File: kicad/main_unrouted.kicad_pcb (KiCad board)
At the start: 2 copper layers, 162.2 x 137.3 mm, 46 parts, among them J1 Barrel_Jack, J2 UART, P1 Mini-DIN_6pins_ver3, SW1 Reset, U1 KM1810VM88, U10 L7805, U11 15 MHz, U12 8255, U13 uSD adapter, U15 74HC148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

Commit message: Add 8259 interrupt controller, update PCB
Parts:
- removed C13: 0.1 uF, footprints:C_Disc_Long
- removed U15: 74HC148, Package_DIP:DIP-16_W7.62mm_Socket
- removed U17: 74HC244, Package_DIP:DIP-20_W7.62mm_Socket
- added U14: 8259, Package_DIP:DIP-28_W15.24mm_Socket, F.Cu at (34.3, 76.2)
- C12: footprint footprints:C_Disc_Long -> footprints:C_Disc_VeryLong
- moved C12 180.2 mm to (41.9, 85.1)
- moved R5 147.3 mm to (23.6, 50.8)
- moved P1 146.6 mm to (30.2, 62.8)
- moved R4 144.8 mm to (23.6, 71.1)
- moved RN1 128.5 mm to (68.6, 119.4)
- moved U13 128.4 mm to (174.6, 113.0), turned to -90 degrees
- moved U18 127.8 mm to (131.9, 113.0)
- moved J2 127.6 mm to (120.7, 152.4)
- moved C9 127.6 mm to (108.6, 135.9)
- moved U16 127.6 mm to (92.7, 143.5)
- moved H1 127.1 mm to (25.4, 149.9)
- moved H2 127.1 mm to (177.8, 149.9)
- moved C11 127.1 mm to (26.7, 134.6)
- moved C14 127.1 mm to (153.7, 25.4)
- moved C6 127.1 mm to (132.0, 66.7)
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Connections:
- U12 pad 14: Net-(U12-PC0) -> INT1
- U16 pad 30: Net-(U16-INTR) -> INT4
- U6 pad 18: unconnected-(U6-I/O/Q-Pad18) -> INT~{EN}
- U8 pad 10: ~{INT1} -> unconnected-(U8-Pad10)
- U8 pad 11: Net-(U12-PC0) -> unconnected-(U8-Pad11)
- U8 pad 12: ~{INT2} -> unconnected-(U8-Pad12)
- U8 pad 13: Net-(U16-INTR) -> unconnected-(U8-Pad13)
- U8 pad 8: ~{INT0} -> unconnected-(U8-Pad8)
- U8 pad 9: Net-(U9-OUT0) -> unconnected-(U8-Pad9)
- U9 pad 10: Net-(U9-OUT0) -> INT0
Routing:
- net GND: track 277.4 -> 252.0 mm
- net +5V: track 191.2 -> 172.9 mm
- net ~{RES}: track 57.1 -> 46.1 mm
- net PS2CLK: track 8.82 -> 6.98 mm
- net PS2DATA: track 13.3 -> 12.6 mm
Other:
- board text added: "Андрій Дунай v0.2, Жовтень 2023 <a@dun.ai>"
- board text removed: "Андрій Дунай v0.2, Вересень 2023 <a@dun.ai>"

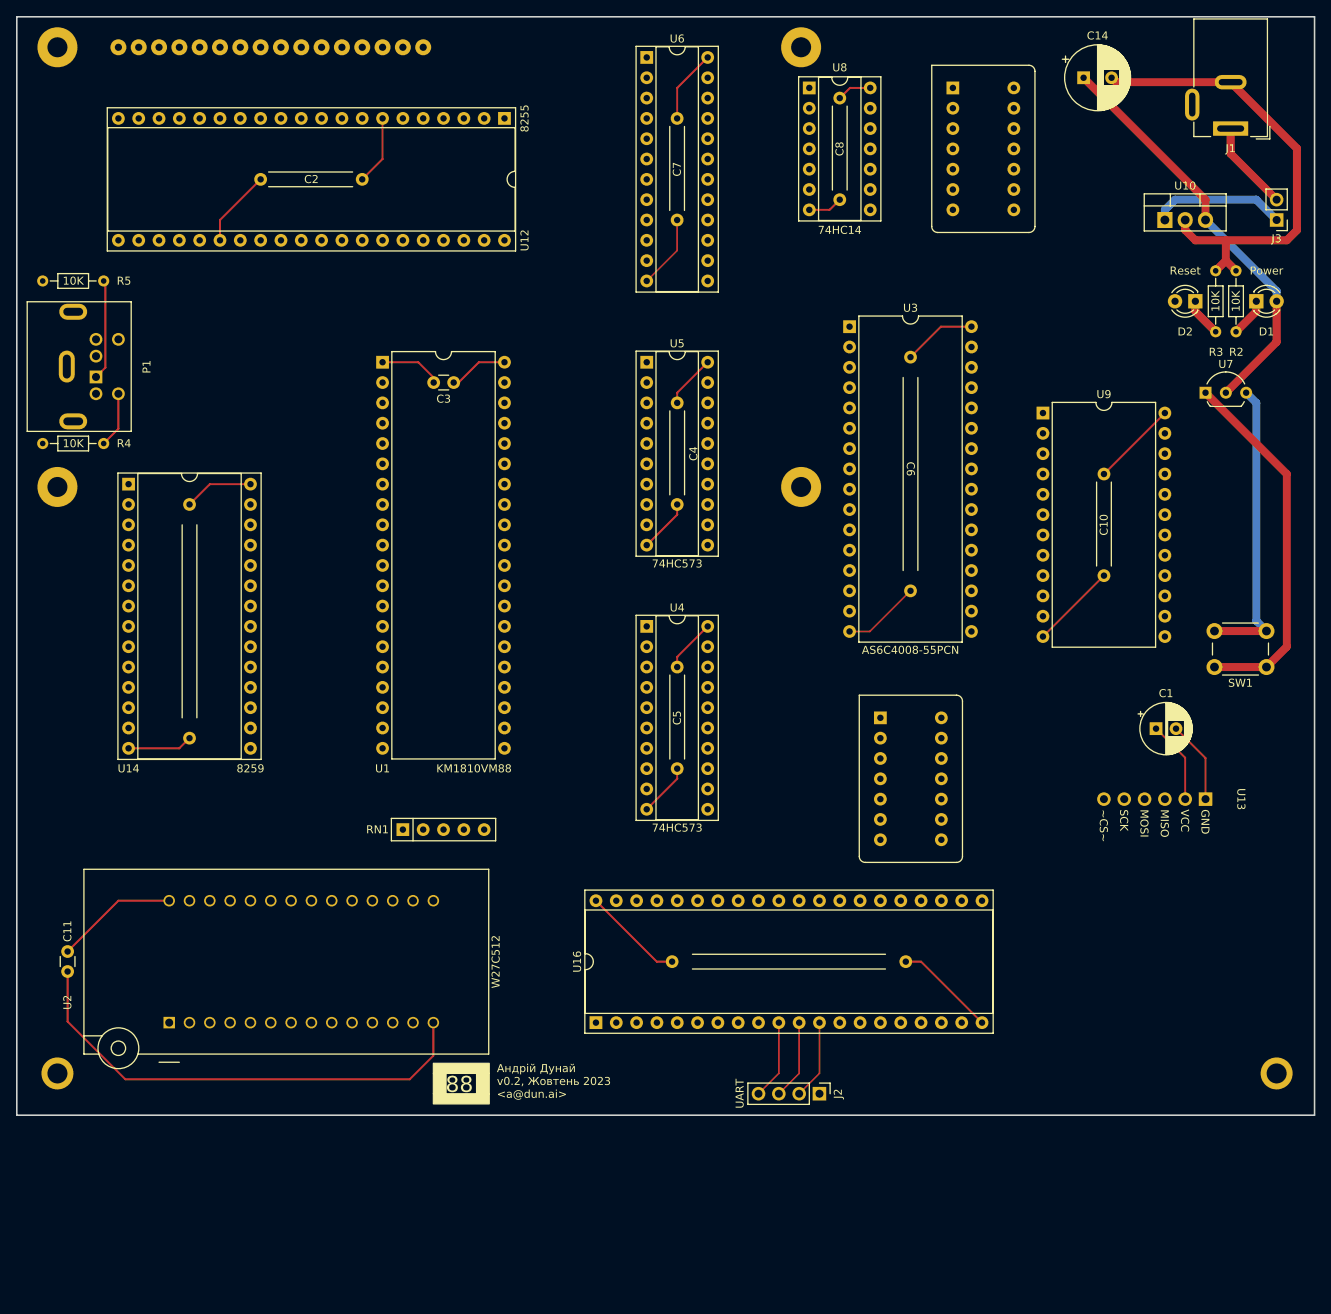
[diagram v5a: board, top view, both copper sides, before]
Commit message: 135x160 board
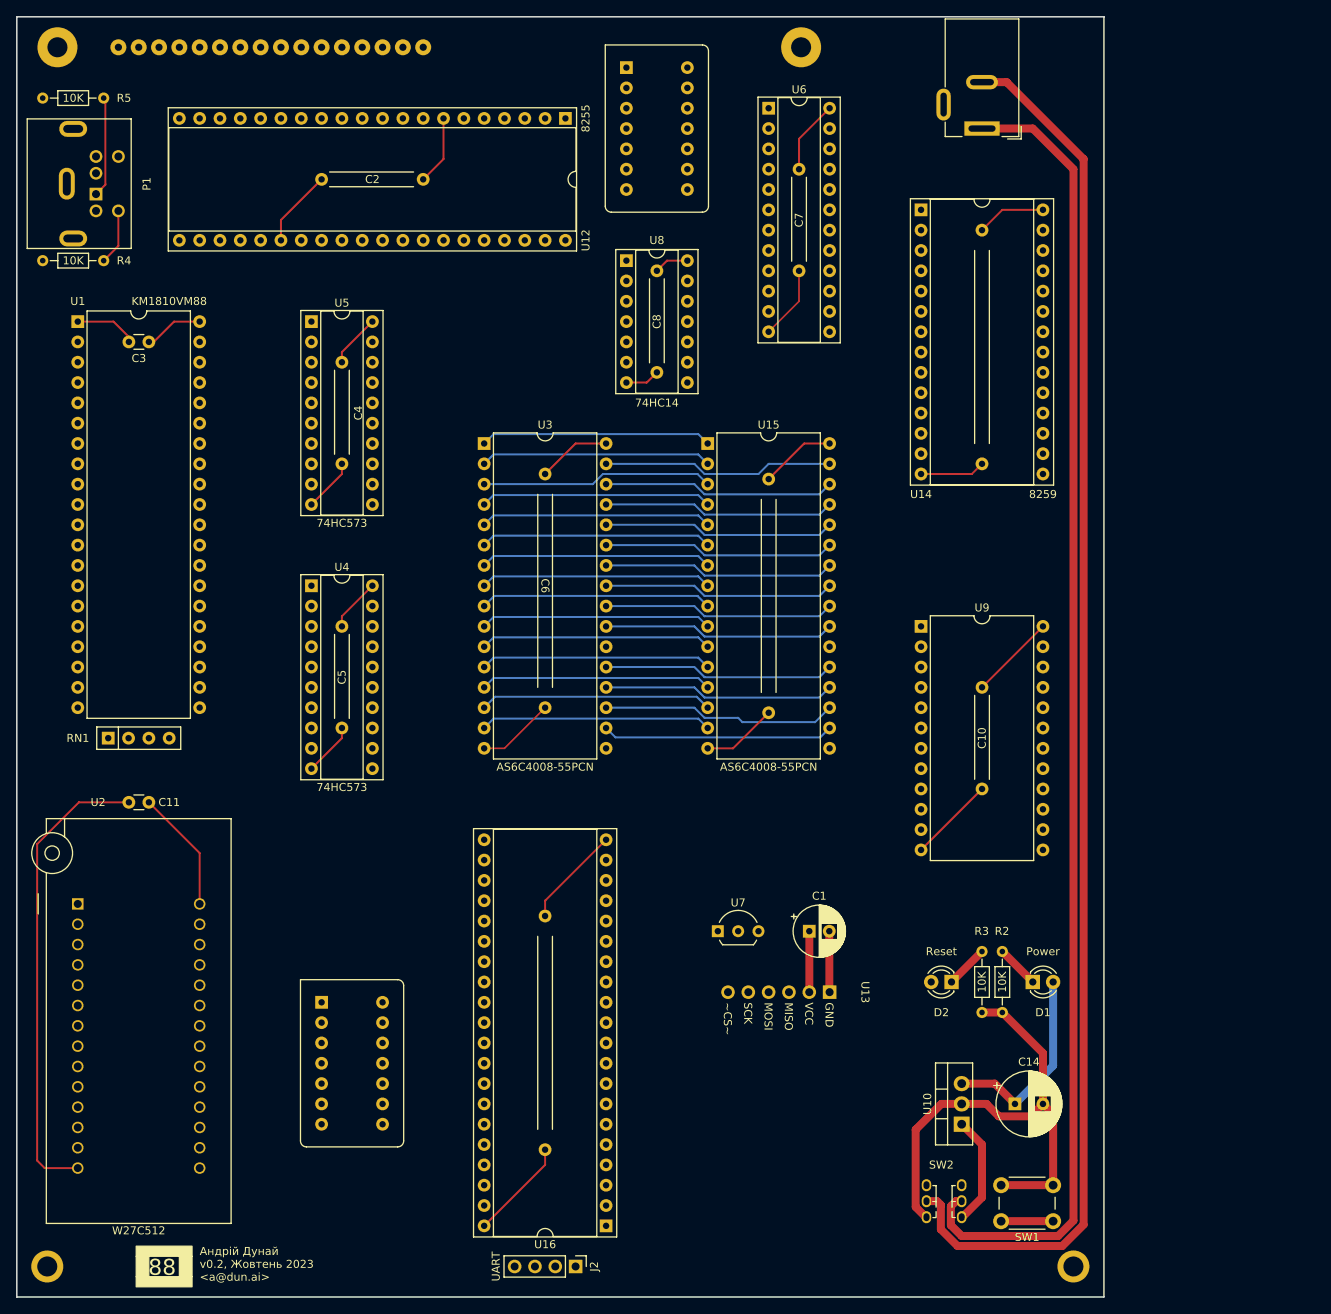
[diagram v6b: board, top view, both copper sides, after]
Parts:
- removed J3: ~, Connector_PinHeader_2.54mm:PinHeader_1x02_P2.54mm_Vertical
- added C13: 0.1 uF, footprints:C_Disc_VeryLong, F.Cu at (114.3, 81.9)
- added SW2: SW_Push_DPDT, footprints:PB22E06, F.Cu at (133.3, 163.0)
- added U15: AS6C4008-55PCN, Package_DIP:DIP-32_W15.24mm, F.Cu at (106.7, 71.1)
- RN1: value 5K -> R_Network03_Split; footprint Resistor_THT:R_Array_SIP5 -> Resistor_THT:R_Array_SIP4
- moved C14 128.6 mm to (145.1, 153.7)
- moved U10 115.8 mm to (138.4, 156.2), turned to 90 degrees
- moved C12 104.8 mm to (141.0, 50.8)
- moved U14 104.8 mm to (133.3, 41.9)
- moved U7 90.8 mm to (108.0, 132.1)
- moved D2 90.4 mm to (137.2, 138.4)
- moved D1 89.6 mm to (147.3, 138.4)
- moved R2 82.8 mm to (143.5, 134.6), turned to -90 degrees
- moved R3 82.8 mm to (141.0, 134.6), turned to -90 degrees
- moved U18 78.4 mm to (62.1, 148.6)
- moved SW1 74.2 mm to (149.9, 168.3)
- moved U13 52.8 mm to (127.6, 137.2)
- moved C1 50.2 mm to (119.4, 132.1)
- moved U3 48.0 mm to (78.7, 71.1)
- moved C6 48.0 mm to (86.4, 81.3)
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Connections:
- J1 pad 2: GND -> Net-(J1-Pad2)
- RN1 pad 4: unconnected-(RN1C-R3.2-Pad4) -> Net-(RN1C-R3.2)
- U1 pad 33: Net-(RN1D-R4.2) -> Net-(RN1C-R3.2)
- U12 pad 6: IO~{EN} -> PPI~{EN}
- U3 pad 22: RAM~{EN} -> LORAM~{EN}
- U6 pad 14: unconnected-(U6-I/O/Q-Pad14) -> HIRAM~{EN}
- U6 pad 15: Net-(U6-I/O/Q-Pad15) -> LORAM~{EN}
- U6 pad 16: Net-(U6-I/O/Q-Pad16) -> ROM~{EN}
- U6 pad 17: unconnected-(U6-I/O/Q-Pad17) -> INT~{EN}
- U6 pad 18: INT~{EN} -> UART~{EN}
- U6 pad 19: UART~{EN} -> TIMER~{EN}
- U6 pad 2: A_{8} -> A_{5}
- U6 pad 20: TIMER~{EN} -> PPI~{EN}
- U6 pad 21: IO~{EN} -> unconnected-(U6-I/O/Q-Pad21)
- U6 pad 22: RAM~{EN} -> Net-(U6-I/O/Q-Pad22)
- U6 pad 23: ROM~{EN} -> Net-(U6-I/O/Q-Pad23)
- U6 pad 3: A_{9} -> A_{6}
- U8 pad 1: Net-(U6-I/O/Q-Pad15) -> Net-(U6-I/O/Q-Pad23)
- U8 pad 2: CLK -> TIMERCLK
- U8 pad 3: Net-(U6-I/O/Q-Pad16) -> Net-(U6-I/O/Q-Pad22)
- U8 pad 4: TIMERCLK -> CLK
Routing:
- net Net-(J1-Pad2): track 0.00 -> 174.7 mm
- net Net-(J1-Pad1): track 11.3 -> 165.6 mm
- net ~{RES}: track 46.1 -> 6.50 mm
- net +5V: track 172.9 -> 142.6 mm
- net AD_{5}: track 0.00 -> 29.4 mm
- net AD_{1}: track 0.00 -> 29.1 mm
- net ~{WR}: track 0.00 -> 29.0 mm
- net A_{8}: track 0.00 -> 29.0 mm
- net A_{15}: track 0.00 -> 29.0 mm
- net AD_{6}: track 0.00 -> 29.0 mm
- net A_{9}: track 0.00 -> 29.0 mm
- net A_{3}: track 0.00 -> 29.0 mm
- net A_{17}: track 0.00 -> 29.0 mm
- net A_{14}: track 0.00 -> 29.0 mm
- net A_{11}: track 0.00 -> 29.0 mm
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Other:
- board size 162.2 x 137.3 mm -> 135.9 x 160 mm

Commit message: PCB 2.0 RC
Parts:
- removed LCD1: ~, footprints:2004A-OLED
- added RV1: R_Potentiometer, Potentiometer_THT:Potentiometer_Bourns_3296Y_Vertical, F.Cu at (207.0, 67.3)
- added U17: T6963C, footprints:LCD24064, F.Cu at (21.8, 17.1)
- added U19: ATF16V8, Package_DIP:DIP-20_W7.62mm_Socket, F.Cu at (73.7, 53.3)
- C1: value 10 uF -> 0.1 uF; footprint Capacitor_THT:CP_Radial_D6.3mm_P2.50mm -> footprints:C_Disc_Long
- U12: footprint Package_DIP:DIP-40_W15.24mm_Socket -> Package_DIP:DIP-40_W15.24mm
- U6: value GAL22V10 -> ATF16V8; footprint Package_DIP:DIP-24_W7.62mm_Socket -> Package_DIP:DIP-20_W7.62mm_Socket
- moved P1 185.6 mm to (215.6, 47.9)
- moved R4 185.6 mm to (209.0, 56.2)
- moved R5 185.6 mm to (209.0, 35.9)
- moved U16 151.4 mm to (142.2, 25.4), turned to 0 degrees
- moved C9 128.5 mm to (149.9, 41.3), turned to -90 degrees
- moved SW2 128.1 mm to (212.1, 61.9)
- moved C2 119.4 mm to (176.5, 55.9), turned to 90 degrees
- moved U10 113.2 mm to (215.9, 73.7), turned to 180 degrees
- moved U18 108.3 mm to (149.9, 85.3), turned to 0 degrees
- moved C14 96.2 mm to (209.9, 82.5)
- moved U7 89.5 mm to (193.0, 104.4), turned to 90 degrees
- moved H2 88.1 mm to (217.2, 114.3)
- moved J2 88.0 mm to (152.4, 111.8)
- moved SW1 86.2 mm to (207.0, 103.8)
- moved U11 84.8 mm to (149.9, 100.5), turned to 0 degrees
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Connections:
- U12 pad 1: Net-(LCD1-D_{3}) -> unconnected-(U12-PA3-Pad1)
- U12 pad 11: Net-(LCD1-E) -> unconnected-(U12-PC6-Pad11)
- U12 pad 12: Net-(LCD1-R~{W}) -> unconnected-(U12-PC5-Pad12)
- U12 pad 13: Net-(LCD1-RS) -> unconnected-(U12-PC4-Pad13)
- U12 pad 2: Net-(LCD1-D_{2}) -> unconnected-(U12-PA2-Pad2)
- U12 pad 3: Net-(LCD1-D_{1}) -> unconnected-(U12-PA1-Pad3)
- U12 pad 37: Net-(LCD1-D_{7}) -> unconnected-(U12-PA7-Pad37)
- U12 pad 38: Net-(LCD1-D_{6}) -> unconnected-(U12-PA6-Pad38)
- U12 pad 39: Net-(LCD1-D_{5}) -> unconnected-(U12-PA5-Pad39)
- U12 pad 4: Net-(LCD1-D_{0}) -> unconnected-(U12-PA0-Pad4)
- U12 pad 40: Net-(LCD1-D_{4}) -> unconnected-(U12-PA4-Pad40)
- U14 pad 1: INT~{EN} -> PIC~{EN}
- U6 pad 10: IO/~{M} -> GND
- U6 pad 11: unconnected-(U6-I-Pad11) -> GND
- U6 pad 12: GND -> unconnected-(U6-I/O-Pad12)
- U6 pad 13: GND -> unconnected-(U6-I/O-Pad13)
- U6 pad 17: INT~{EN} -> unconnected-(U6-I/O-Pad17)
- U6 pad 18: UART~{EN} -> Net-(U6-I/O-Pad18)
- U6 pad 19: TIMER~{EN} -> Net-(U6-I/O-Pad19)
- U6 pad 2: A_{5} -> A_{16}
- U6 pad 20: PPI~{EN} -> +5V
- U6 pad 3: A_{6} -> A_{17}
- U6 pad 4: A_{16} -> A_{18}
- U6 pad 5: A_{17} -> A_{19}
- U6 pad 6: A_{18} -> IO/~{M}
- U6 pad 7: A_{19} -> unconnected-(U6-I-Pad7)
- U6 pad 8: ~{RD} -> unconnected-(U6-I-Pad8)
- U6 pad 9: ~{WR} -> unconnected-(U6-I-Pad9)
- U8 pad 1: Net-(U6-I/O/Q-Pad23) -> Net-(U6-I/O-Pad19)
- U8 pad 3: Net-(U6-I/O/Q-Pad22) -> Net-(U6-I/O-Pad18)
- U9 pad 21: TIMER~{EN} -> PIT~{EN}
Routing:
- net Net-(J1-Pad2): track 174.7 -> 0.00 mm
- net Net-(J1-Pad1): track 165.6 -> 0.00 mm
- net AD_{5}: track 29.4 -> 0.00 mm
- net AD_{1}: track 29.1 -> 0.00 mm
- net ~{WR}: track 29.0 -> 0.00 mm
- net A_{8}: track 29.0 -> 0.00 mm
- net A_{15}: track 29.0 -> 0.00 mm
- net AD_{6}: track 29.0 -> 0.00 mm
- net A_{9}: track 29.0 -> 0.00 mm
- net A_{3}: track 29.0 -> 0.00 mm
- net A_{17}: track 29.0 -> 0.00 mm
- net A_{14}: track 29.0 -> 0.00 mm
- net A_{11}: track 29.0 -> 0.00 mm
- net A_{10}: track 29.0 -> 0.00 mm
- net ~{RD}: track 29.0 -> 0.00 mm
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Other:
- board size 135.9 x 160 mm -> 200 x 100 mm

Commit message: Cleaner PCB
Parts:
- H1, H2: footprint footprints:Hole_2.5x4 -> footprints:Hole_3.5x5
- moved RN1 3.59 mm to (34.9, 80.0)
- moved C1 2.54 mm to (80.0, 58.4)
- moved C7 2.54 mm to (80.0, 27.9)
- moved U19 2.54 mm to (76.2, 53.3)
- moved U3 2.54 mm to (94.0, 25.4)
- moved U6 2.54 mm to (76.2, 22.9)
- moved U1 2.54 mm to (31.1, 25.4)
- moved C3 2.54 mm to (40.0, 27.9)
- moved C4 2.54 mm to (62.2, 27.9)
- moved C5 2.54 mm to (62.2, 58.4)
- moved U4 2.54 mm to (58.4, 53.3)
- moved U5 2.54 mm to (58.4, 22.9)
- moved C14 2.54 mm to (212.4, 82.5)
- moved C6 2.54 mm to (101.6, 35.6)
- moved D1 1.27 mm to (205.7, 90.2)
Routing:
- net Net-(J1-Pad2): track 0.00 -> 55.6 mm
- net Net-(J1-Pad1): track 0.00 -> 43.6 mm
- net GND: track 207.3 -> 216.5 mm
- net Net-(U10-IN): track 0.00 -> 7.42 mm
- net +5V: track 158.1 -> 159.7 mm
